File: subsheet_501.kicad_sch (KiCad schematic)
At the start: 14 parts, among them U509 74LS244_PHY, U510 74LS244_PHY, U511 74LS373_PHY, U512 74LS244_PHY

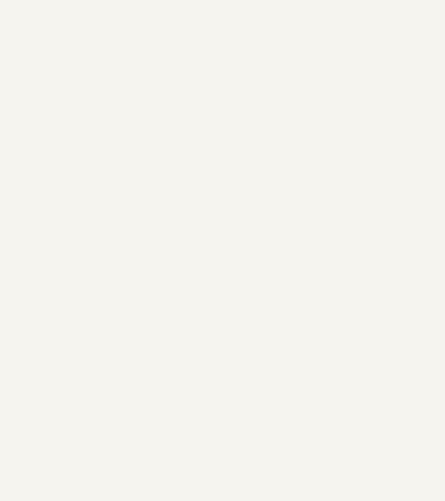
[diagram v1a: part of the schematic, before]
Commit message: add gnd/vcc symbol to start replacing local labels
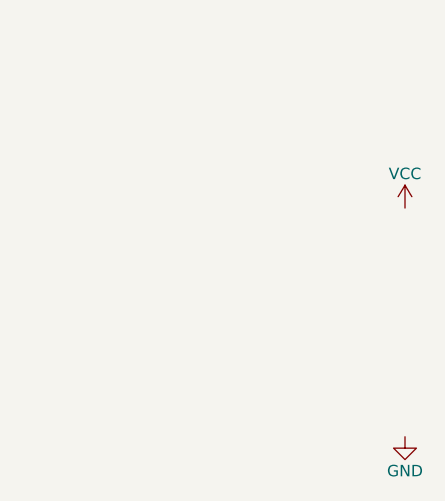
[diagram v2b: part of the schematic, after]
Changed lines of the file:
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@@
     (pin "8")
   )
+  (symbol (lib_id "power:GND") (at 186.69 240.03 0) (unit 1)
+    (in_bom yes) (on_board yes)
+    (property "Reference" "#PWR?" (id 0) (at 186.69 246.38 0)
+      (effects (font (size 1.27 1.27)) hide)
+    )
+    (property "Value" "GND" (id 1) (at 186.69 243.84 0))
+    (property "Footprint" "" (id 2) (at 186.69 240.03 0)
+      (effects (font (size 1.27 1.27)) hide)
+    )
+    (property "Datasheet" "" (id 3) (at 186.69 240.03 0)
+      (effects (font (size 1.27 1.27)) hide)
+    )
+    (pin "1")
+  )
+  (symbol (lib_id "power:VCC") (at 186.69 214.63 0) (unit 1)
+    (in_bom yes) (on_board yes)
+    (property "Reference" "#PWR?" (id 0) (at 186.69 218.44 0)
+      (effects (font (size 1.27 1.27)) hide)
+    )
+    (property "Value" "VCC" (id 1) (at 186.69 210.82 0))
+    (property "Footprint" "" (id 2) (at 186.69 214.63 0)
+      (effects (font (size 1.27 1.27)) hide)
+    )
+    (property "Datasheet" "" (id 3) (at 186.69 214.63 0)
+      (effects (font (size 1.27 1.27)) hide)
+    )
+    (pin "1")
+  )
 )
